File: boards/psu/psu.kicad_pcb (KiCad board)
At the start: 2 copper layers, 94 x 50.8 mm, 18 parts, among them IC1 NSD10-12D12, J1 Conn_02x04_Odd_Even, J2 Conn_02x05_Odd_Even

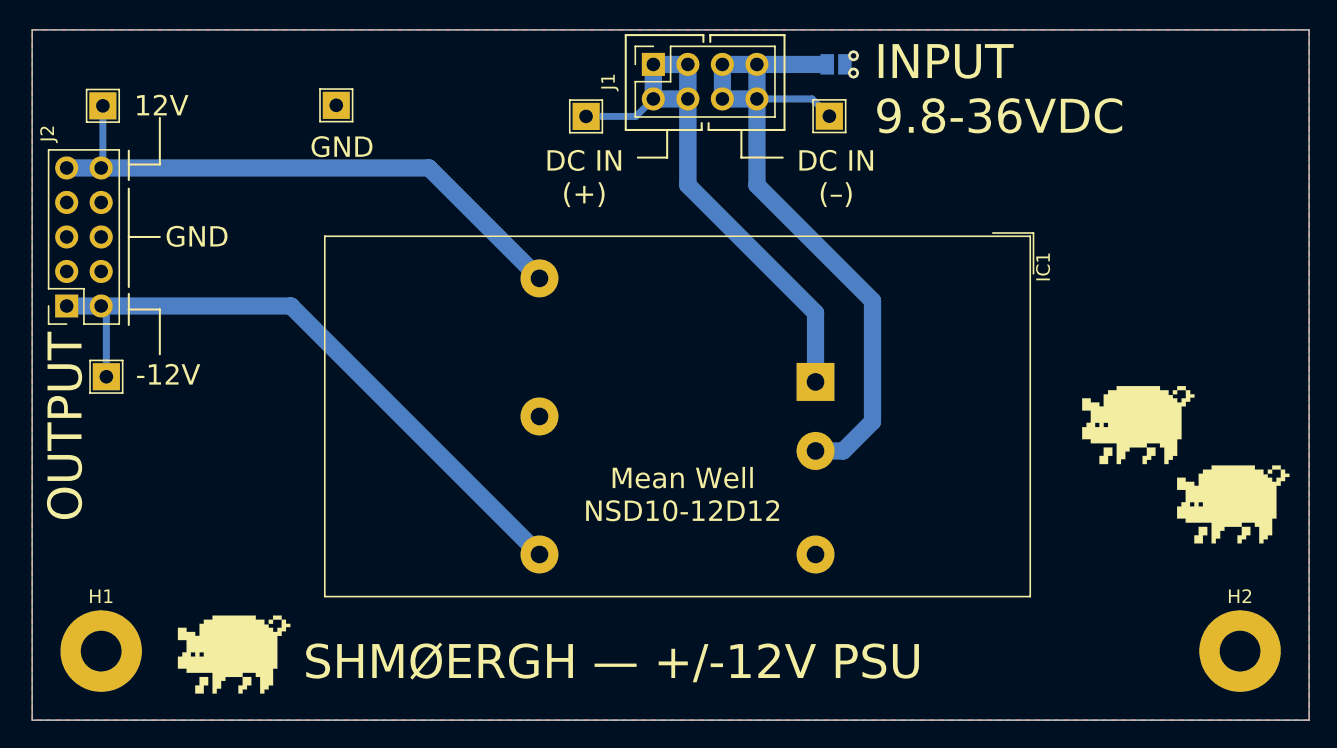
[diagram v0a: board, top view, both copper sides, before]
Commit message: Fixed PSU and UI sizing bug
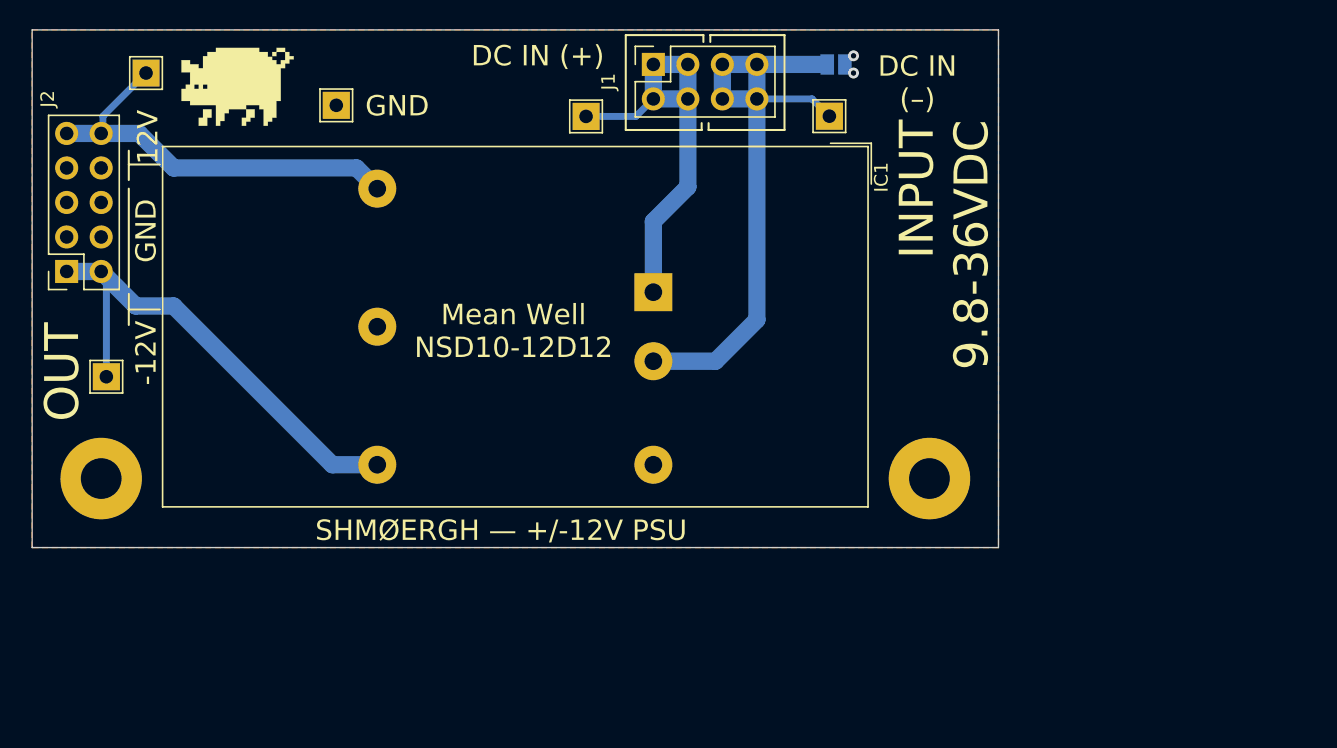
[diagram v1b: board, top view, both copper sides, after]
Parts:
- removed the G*** at (108.8, 109.5)
- removed the G*** at (175.4, 92.6)
- removed the G*** at (122.2, 85.3)
- moved G*** 79.5 mm to (109.1, 67.7)
- moved G*** 49.4 mm to (131.7, 79.6)
- moved G*** 48.2 mm to (127.5, 86.1)
- moved H2 26.2 mm to (160.0, 96.5)
- moved IC1 13.6 mm to (139.7, 82.8)
- moved G*** 13.5 mm to (112.3, 79.4)
- moved H1 12.7 mm to (99.1, 96.5)
- moved TP3 3.99 mm to (102.4, 66.7)
- moved J2 2.54 mm to (96.5, 81.3)
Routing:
- net +12V: track 42.8 -> 30.4 mm
- net -12V: track 47.7 -> 36.7 mm
- net DC_IN_+: track 40.4 -> 30.9 mm
- net DC_IN_-: track 53.3 -> 46.0 mm
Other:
- board size 94 x 50.8 mm -> 71.1 x 38.1 mm
- board text added: "OUT"
- board text removed: "OUTPUT"
